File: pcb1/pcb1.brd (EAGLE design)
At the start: 101.6 x 53.3 mm, 29 parts, among them J1 12V, J2 24V, J3 RTD, J4 SPT25, J5 SPT25, J6 SPDT25, J7 TMP006, J8 VN-200, Q1 SI01P10-TP, Q2 SI01P10-TP

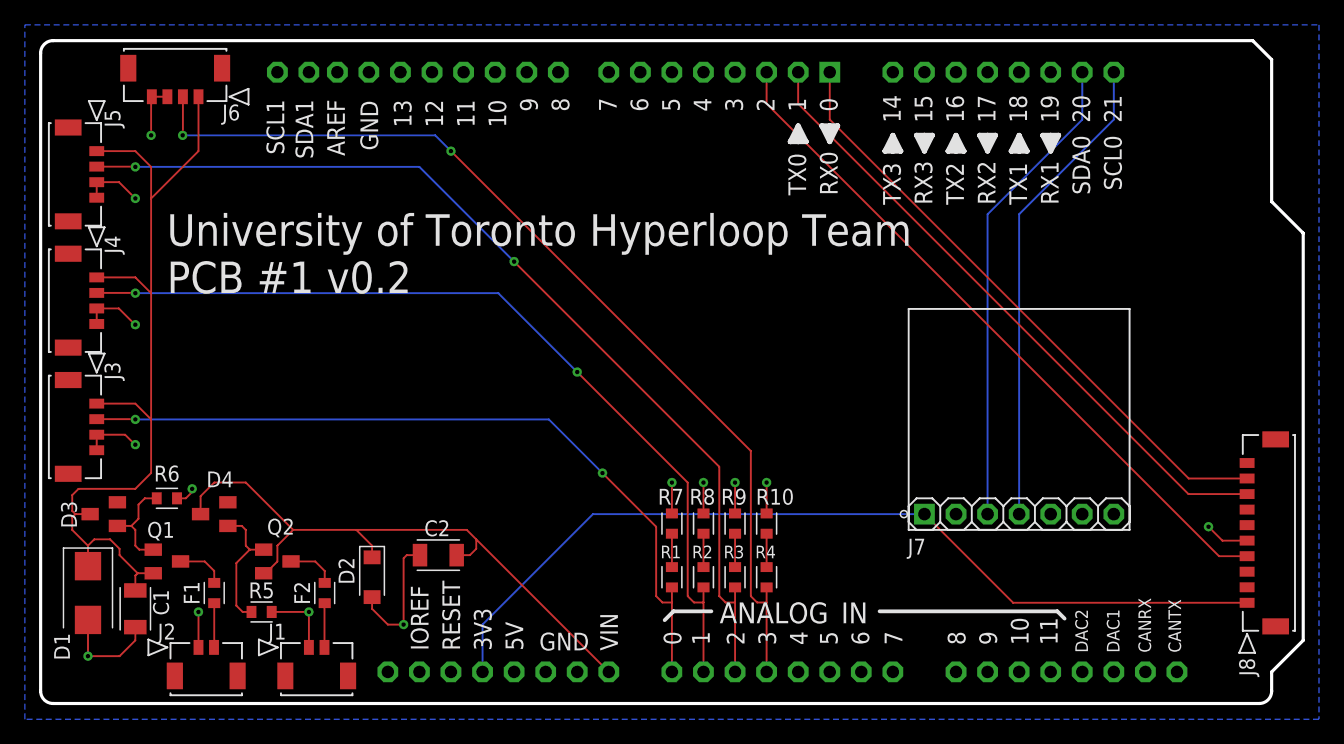
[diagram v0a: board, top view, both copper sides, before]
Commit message: Changed TMP006 Connection
* changed tmp006 connection to molex 4pin
+ Added SDA/SCL pullup resistors
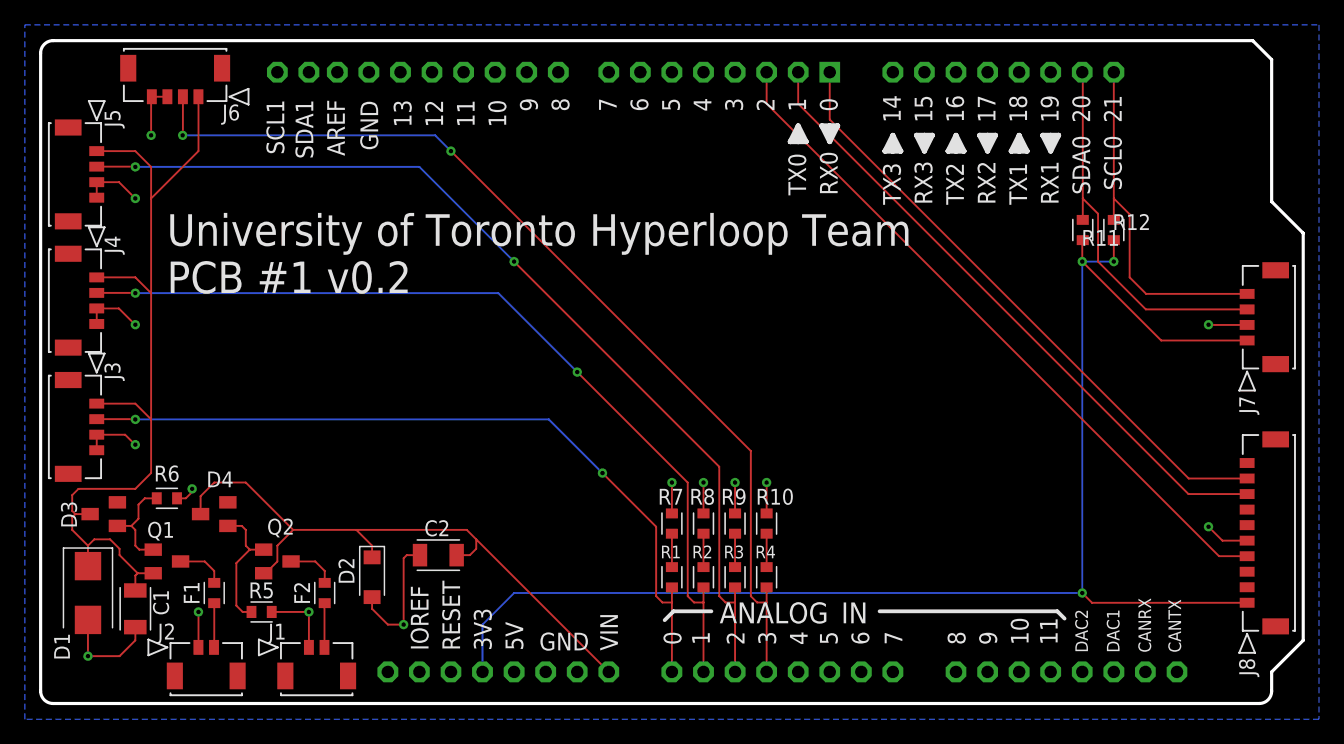
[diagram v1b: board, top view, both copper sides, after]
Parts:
- added R11, R12: 10k, Resistor:RESC1608X60
- J7: device Female Pin Headers:1X07 -> Molex Micro-Lock PLUS:4PIN
- moved J7 23.1 mm to (97.1, 29.2), turned to 270 degrees
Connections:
- net +3.3V: now also R11.2, R12.2
- net SCL: now also R12.1
- net SDA: now also R11.1
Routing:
- net +3.3V: track 72.0 -> 115.3 mm, vias 0 -> 3
- net SCL: track 38.7 -> 28.8 mm
- net SDA: track 38.7 -> 31.1 mm
- net GND: track 61.9 -> 65.0 mm, vias 14 -> 15
